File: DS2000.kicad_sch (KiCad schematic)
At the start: 56 parts, among them J1 USB-C, J3 USB wire, SW1 MUTE, SW2 DEAFEN, SW3 DISCONNECT, U1 USBLC6-2SC6, U2 AP2112K-3.3, U3 RP2350A, U4 W25Q32JVSS, U5 74AHCT1G125, Y1 12MHz

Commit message: feat: switch to Kailh Choc V1 low-profile keys
- SW_Kailh_Choc_V1_1.00u footprint in the project library, generated from Kailh's CPG1350
  drawing (geometry matches kiswitch, MIT); courtyard on the 13.8 mm lower housing
- own STEP models for the Choc V1 switch and an MBK-style keycap
- 18 mm key pitch, key row 1 mm forward, LEDs 4.7 mm south of each switch centre
- board re-placed and re-routed with the pipeline; ERC/parity clean, DRC only the known
  text_thickness and lib_footprint_mismatch warnings
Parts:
- SW1, SW2, SW3: footprint Button_Switch_Keyboard:SW_Cherry_MX_1.00u_PCB -> DS2000:SW_Kailh_Choc_V1_1.00u
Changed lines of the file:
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@@
 		(rev "A")
 		(company "Mechardo Labs")
-		(comment 1 "RP2350A, 3x MX keys, SK6812MINI-E per key, USB-C")
+		(comment 1 "RP2350A, 3x Choc V1 keys, SK6812MINI-E per key, USB-C")
 		(comment 2 "Pinout follows DS-2000-Firmware/include/pins.h")
 	)
@@
 			)
 		)
-		(property "Footprint" "Button_Switch_Keyboard:SW_Cherry_MX_1.00u_PCB"
+		(property "Footprint" "DS2000:SW_Kailh_Choc_V1_1.00u"
 			(at 238.76 139.7 0)
 			(hide yes)
@@
 			)
 		)
-		(property "Footprint" "Button_Switch_Keyboard:SW_Cherry_MX_1.00u_PCB"
+		(property "Footprint" "DS2000:SW_Kailh_Choc_V1_1.00u"
 			(at 238.76 132.08 0)
 			(hide yes)
@@
 			)
 		)
-		(property "Footprint" "Button_Switch_Keyboard:SW_Cherry_MX_1.00u_PCB"
+		(property "Footprint" "DS2000:SW_Kailh_Choc_V1_1.00u"
 			(at 238.76 124.46 0)
 			(hide yes)

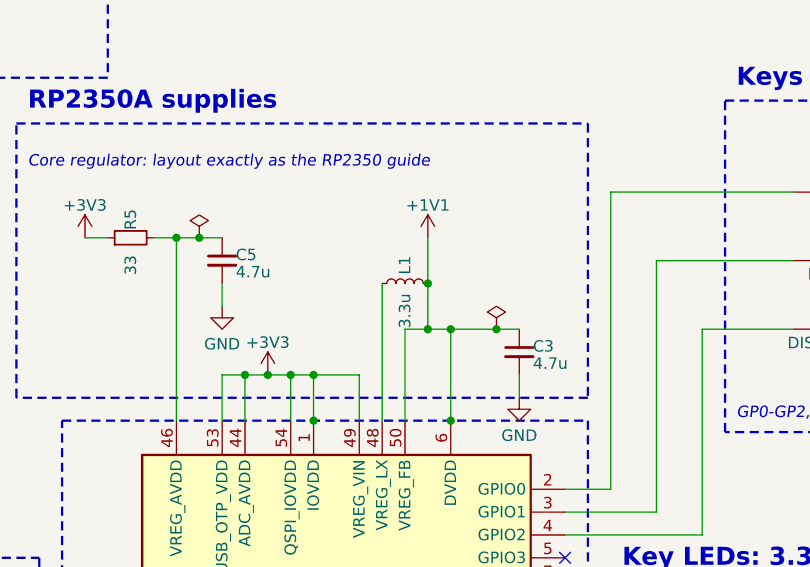
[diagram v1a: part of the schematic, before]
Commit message: fix: copy the RP2350A minimal design's core regulator layout
Raspberry Pi says the regulator layout should be copied, not improvised: the inductor's field upsets
the output capacitor when placed or oriented differently. The autorouted rev A had L1 4.6 mm away
on a 0.2 mm VREG_LX track, the output cap past the inductor and VREG_AVDD running under it.

- L1, C3, C4, C5 and C16 at the reference's offsets from VREG_LX (pin 48), from their KiCad files
  (RPI-RP2350A-MINIMAL R4-S1, MIT); hand routing in preroute.py, their four small pours in
  vreg_pours.py
- L1 footprint for the Abracon AOTA-B201610S3R3-101-T with its polarity dot; the schematic symbol
  turned so pin 1 (the dot) is +1V1, as in the reference
- the reference's wide 0402 land for the two 4.7 uF caps, so VREG_LX runs between them
- RP2350A cluster 0.5 mm lower and R5 beside C5 so everything clears J1's pegs and shell pins
- USB series resistors and C16 where the reference has them; +3V3 for pins 49/53/54 under the
  package as in the reference
- exposed pad joined solidly to the planes; Choc silkscreen moved inside the parts' clearance
- fanout.py keeps hand-routed pads
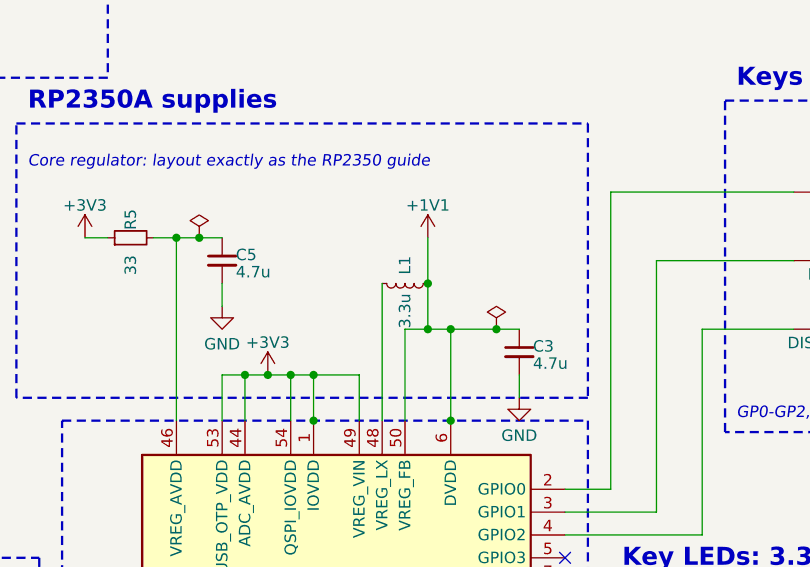
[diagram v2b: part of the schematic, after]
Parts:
- C3, C4: footprint Capacitor_SMD:C_0402_1005Metric -> DS2000:C_0402_1005Metric_Wide
- L1: footprint Inductor_SMD:L_Murata_DFE201610P -> DS2000:L_Abracon_AOTA-B201610S3R3-101-T; Note Polarity-marked; orientation and layout per RP2350 guide. V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 -> Polarity dot = pin 1 = +1V1. Layout copied from the RP2350A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
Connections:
- net +1V1: now also L1.1; no longer L1.2
- net at U3.48 (VREG_LX): now also L1.2; no longer L1.1
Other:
- moved on the sheet: L1
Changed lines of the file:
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@@
 			)
 		)
-		(property "Footprint" "Capacitor_SMD:C_0402_1005Metric"
+		(property "Footprint" "DS2000:C_0402_1005Metric_Wide"
 			(at 204.72 143.51 0)
 			(hide yes)
@@
 	(symbol
 		(lib_id "Device:L_Small")
-		(at 190.5 134.62 90)
+		(at 190.5 134.62 270)
 		(unit 1)
 		(body_style 1)
@@
 			)
 		)
-		(property "Footprint" "Inductor_SMD:L_Murata_DFE201610P"
+		(property "Footprint" "DS2000:L_Abracon_AOTA-B201610S3R3-101-T"
 			(at 190.5 137.66 0)
 			(hide yes)
@@
 			)
 		)
-		(property "Note" "Polarity-marked; orientation and layout per RP2350 guide. Verify pads"
+		(property "Note" "Polarity dot = pin 1 = +1V1. Layout copied from the RP2350A minimal design (R4-S1)"
 			(at 190.5 137.66 0)
 			(hide yes)
@@
 			)
 		)
-		(property "Footprint" "Capacitor_SMD:C_0402_1005Metric"
+		(property "Footprint" "DS2000:C_0402_1005Metric_Wide"
 			(at 80.26 271.78 0)
 			(hide yes)

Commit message: feat: BOM with LCSC numbers and JLCPCB fabrication outputs in CI
- tools/bom/set_fields.py: the parts table for assembly (MPN, manufacturer, LCSC), each number
  checked on its LCSC/JLCPCB page or taken from the RP2350A minimal design's BOM; writes the fields
  into the schematic and onto the board's footprints (schematic parity stays clean)
- F1 is now the 15 V 1206L050/15YR (same 500 mA hold), for margin on VBUS
- kibot/fab.kibot.yaml: KiBot's JLCPCB template (gerbers, drill, BOM, CPL with rotation fixes,
  zip) and the board's STEP with its origin at the board centre (grid origin set to 100, 94)
- CI builds them on every change; DRC and parity now fail the job on any new error
- design doc: BOM table with LCSC numbers and what to choose and check when ordering
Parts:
- C1, C2: LCSC (none) -> C15850; MPN (none) -> CL21A106KAYNNNE; Manufacturer (none) -> Samsung Electro-Mechanics
- C10, C11, C12, C13, C14, C15, C16, C19, C20, C21, C22, C6, C7, C8, C9: LCSC (none) -> C1525; MPN (none) -> CL05B104KO5NNNC; Manufacturer (none) -> Samsung Electro-Mechanics
- C17, C18: LCSC (none) -> C1548; MPN (none) -> 0402CG150J500NT; Manufacturer (none) -> FH
- C3, C4, C5: LCSC (none) -> C82453; MPN (none) -> GRM155R60J475ME47D; Manufacturer (none) -> Murata
- D1, D2: LCSC (none) -> C5149201
- F1: LCSC (none) -> C151162; MPN 1206L050YR -> 1206L050/15YR
- J1: LCSC (none) -> C165948
- L1: LCSC (none) -> C42411119
- R1, R2: LCSC (none) -> C25905; MPN (none) -> 0402WGF5101TCE; Manufacturer (none) -> UNI-ROYAL
- R10: LCSC (none) -> C25076; MPN (none) -> 0402WGF1000TCE; Manufacturer (none) -> UNI-ROYAL
- R3, R4: LCSC (none) -> C138021; MPN (none) -> RC0402FR-0727RL; Manufacturer (none) -> Yageo
- R5: LCSC (none) -> C138002; MPN (none) -> RC0402FR-0733RL; Manufacturer (none) -> Yageo
- R6, R8: LCSC (none) -> C11702; MPN (none) -> 0402WGF1001TCE; Manufacturer (none) -> UNI-ROYAL
- R7, R9: LCSC (none) -> C25744; MPN (none) -> 0402WGF1002TCE; Manufacturer (none) -> UNI-ROYAL
- U1: LCSC (none) -> C7519
- U2: LCSC (none) -> C51118
- U3: LCSC (none) -> C42411118
- U4: LCSC (none) -> C179173
- U5: LCSC (none) -> C12495; MPN 74AHCT1G125GW -> 74AHCT1G125GW,125
- Y1: LCSC (none) -> C20625731
